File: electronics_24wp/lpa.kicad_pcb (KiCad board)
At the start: 2 copper layers, 143 x 74 mm, 87 parts, among them IC1 ATMEGA328-A, P1 CONN_2, P2 CONN_3X2, U1 SD_CARD, U2 LD1117S33, U3 TLC5941, U4 TLC5941, U5 TLC5941, Y1 RESONATEUR

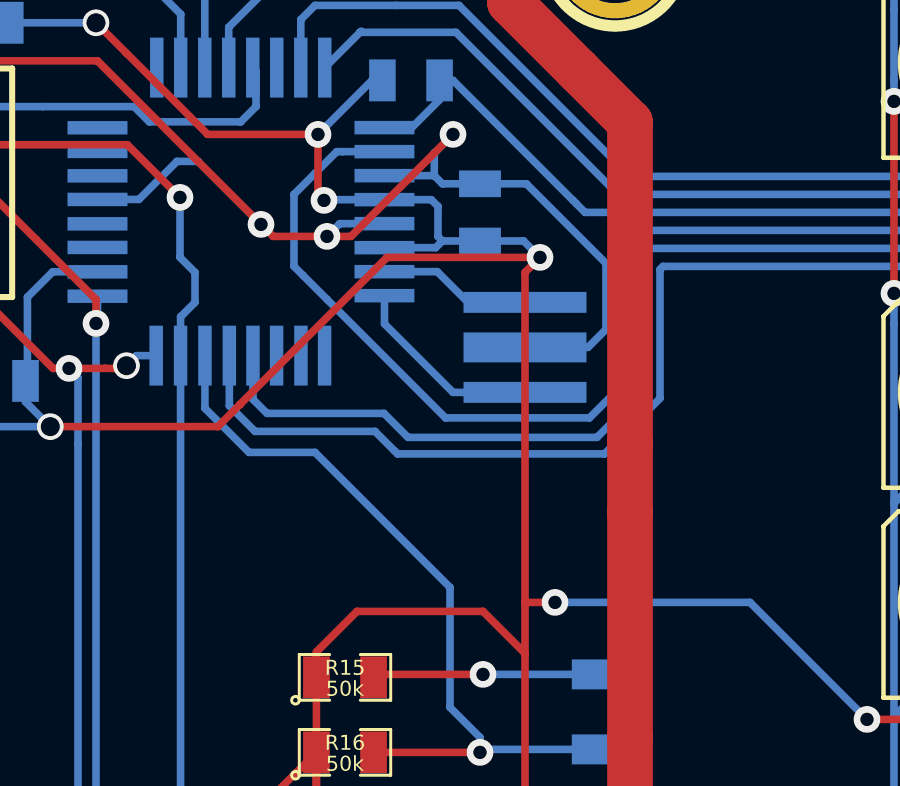
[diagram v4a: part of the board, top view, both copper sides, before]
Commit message: Changed board to use quartz oscillator.
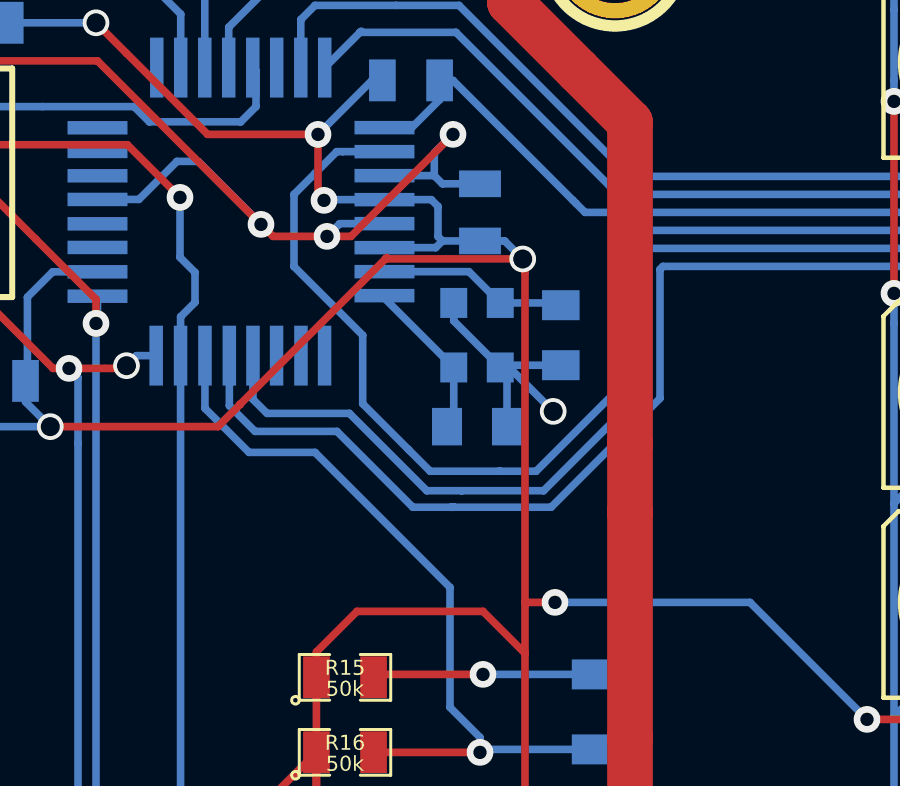
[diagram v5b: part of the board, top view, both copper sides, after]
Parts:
- removed Y1: RESONATEUR, crystal_smd
- added C10: 12pF, Capacitors_SMD:C_0805, B.Cu at (88.9, 120.1)
- added C9: 12pF, Capacitors_SMD:C_0805, B.Cu at (91.7, 117.1)
- added X1: CRYSTAL_SMD, LPA_parts:Crystal_SMD_3.2_2.5_4pins, B.Cu at (88.9, 117.1)
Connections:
- IC1 pad 10: (no net) -> Net-(IC1-Pad10)
- IC1 pad 11: (no net) -> Net-(IC1-Pad11)
- IC1 pad 19: (no net) -> Net-(IC1-Pad19)
- IC1 pad 20: (no net) -> Net-(IC1-Pad20)
- IC1 pad 22: (no net) -> Net-(IC1-Pad22)
- IC1 pad 23: (no net) -> Net-(IC1-Pad23)
- IC1 pad 24: (no net) -> Net-(IC1-Pad24)
- IC1 pad 25: (no net) -> Net-(IC1-Pad25)
- IC1 pad 30: (no net) -> Net-(IC1-Pad30)
- IC1 pad 9: (no net) -> Net-(IC1-Pad9)
- U3 pad : GND -> (no net)
- U3 pad 23: (no net) -> Net-(U3-Pad23)
- U4 pad : GND -> (no net)
- U4 pad 23: (no net) -> Net-(U4-Pad23)
- U5 pad : GND -> (no net)
- U5 pad 23: (no net) -> Net-(U5-Pad23)
- U5 pad 24: (no net) -> Net-(U5-Pad24)
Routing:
- net Net-(U5-Pad24): track 0.00 -> 30.9 mm, vias 0 -> 4
- net (no net): track 30.9 -> 0.00 mm, vias 4 -> 0
- net /tlcs_1-3/SCLK: track 218.0 -> 220.8 mm
- net /tlcs_1-3/XLAT: track 202.6 -> 204.2 mm
- net /tlcs_1-3/GSCLK: track 290.9 -> 292.4 mm
- net /tlcs_1-3/VCC: track 311.6 -> 310.3 mm
- net Net-(C9-Pad2): track 5.11 -> 6.34 mm
- net GND: track 147.2 -> 146.1 mm, vias 7 -> 8
- net Net-(C10-Pad2): track 6.57 -> 5.42 mm

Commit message: Improved footprint of TLCs.
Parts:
- U3, U4, U5: footprint TLC5940_THERMVIAS2 -> LPA_parts:TLC5940_THERMVIAS

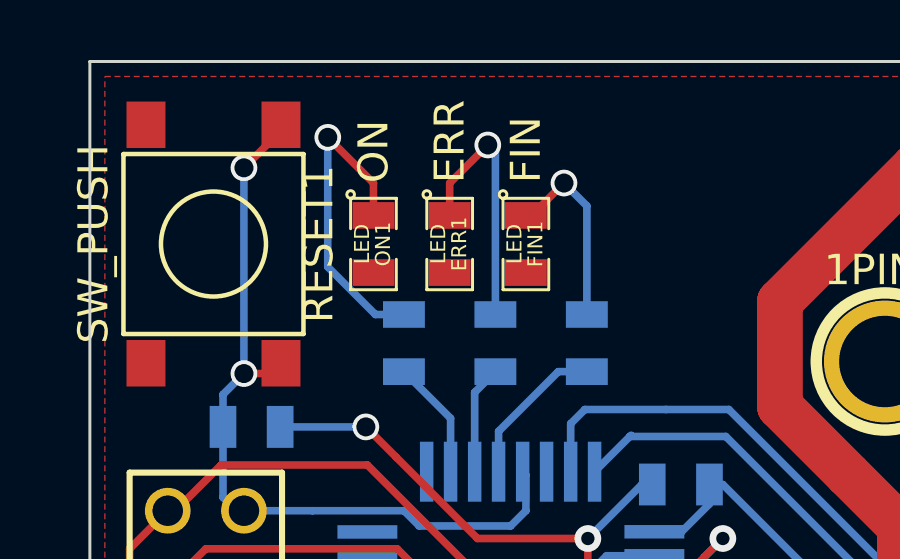
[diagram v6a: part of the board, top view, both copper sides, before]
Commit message: Streamlined library files for the electronic schematic.
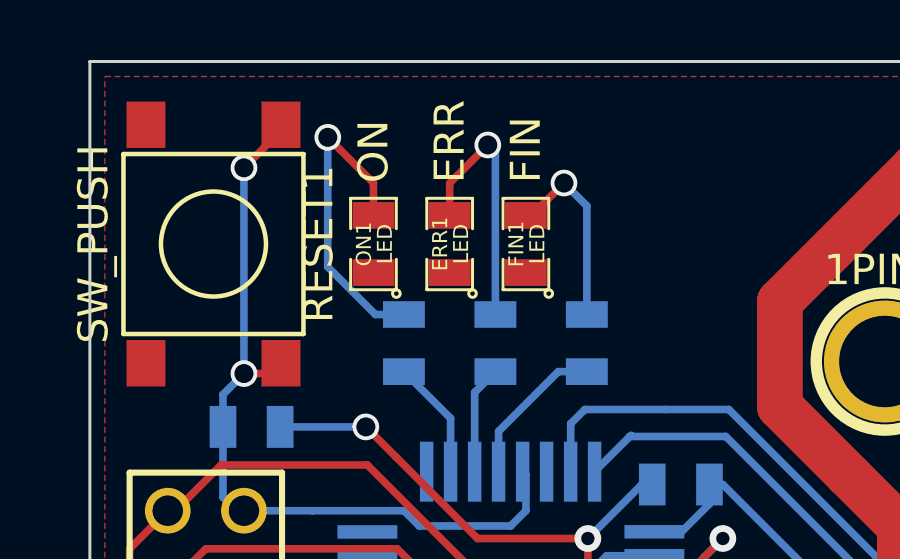
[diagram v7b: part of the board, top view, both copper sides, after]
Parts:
- turned ERR1 to 90 degrees
- turned FIN1 to 90 degrees
- turned ON1 to 90 degrees
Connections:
- ERR1 pad 1: Net-(ERR1-Pad1) -> GND
- ERR1 pad 2: GND -> Net-(ERR1-Pad2)
- FIN1 pad 1: Net-(FIN1-Pad1) -> GND
- FIN1 pad 2: GND -> Net-(FIN1-Pad2)
- ON1 pad 1: Net-(ON1-Pad1) -> GND
- ON1 pad 2: GND -> Net-(ON1-Pad2)
- R_ERR1 pad 2: Net-(ERR1-Pad1) -> Net-(ERR1-Pad2)
- R_FIN1 pad 2: Net-(FIN1-Pad1) -> Net-(FIN1-Pad2)
- R_ON1 pad 2: Net-(ON1-Pad1) -> Net-(ON1-Pad2)
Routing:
- net Net-(ON1-Pad2): track 0.00 -> 10.8 mm, vias 0 -> 1
- net Net-(ON1-Pad1): track 10.8 -> 0.00 mm, vias 1 -> 0
- net Net-(ERR1-Pad2): track 0.00 -> 8.63 mm, vias 0 -> 1
- net Net-(ERR1-Pad1): track 8.63 -> 0.00 mm, vias 1 -> 0
- net Net-(FIN1-Pad2): track 0.00 -> 6.48 mm, vias 0 -> 1
- net Net-(FIN1-Pad1): track 6.48 -> 0.00 mm, vias 1 -> 0

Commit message: Assigned footprint to LED sockets.
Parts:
- D1, D10, D11, D12, D13, D14, D15, D16, D17, D18, D19, D2, D20, D21, D22, D23, D24, D25, D26, D27, D28, D29, D3, D30, D31, D32, D33, D34, D35, D36, D37, D38, D39, D4, D40, D41, D42, D43, D44, D45, D46, D47, D48, D5, D6, D7, D8, D9: footprint PCV220_LEDSOCKET -> LPA_parts:PCV220_LEDSOCKET
